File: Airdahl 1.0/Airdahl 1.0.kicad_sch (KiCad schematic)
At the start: 59 parts, among them J1 Conn_01x04, J2 DF40C-34DS-0.4V_58_, J3 DF40C-34DS-0.4V_58_, J4 USB_C_Receptacle_USB2.0_16P, SW1 SW_MEC_5E, SW2 SW_MEC_5E, U1 STM32F446RETx, U2 MCP2200-I-MQ, U3 LT1963AxST-3.3, Y1 ABM3B-8.000MHZ-12-D1X-T, Y2 ABS25-32.768KHZ-6-T, Y3 12MHz

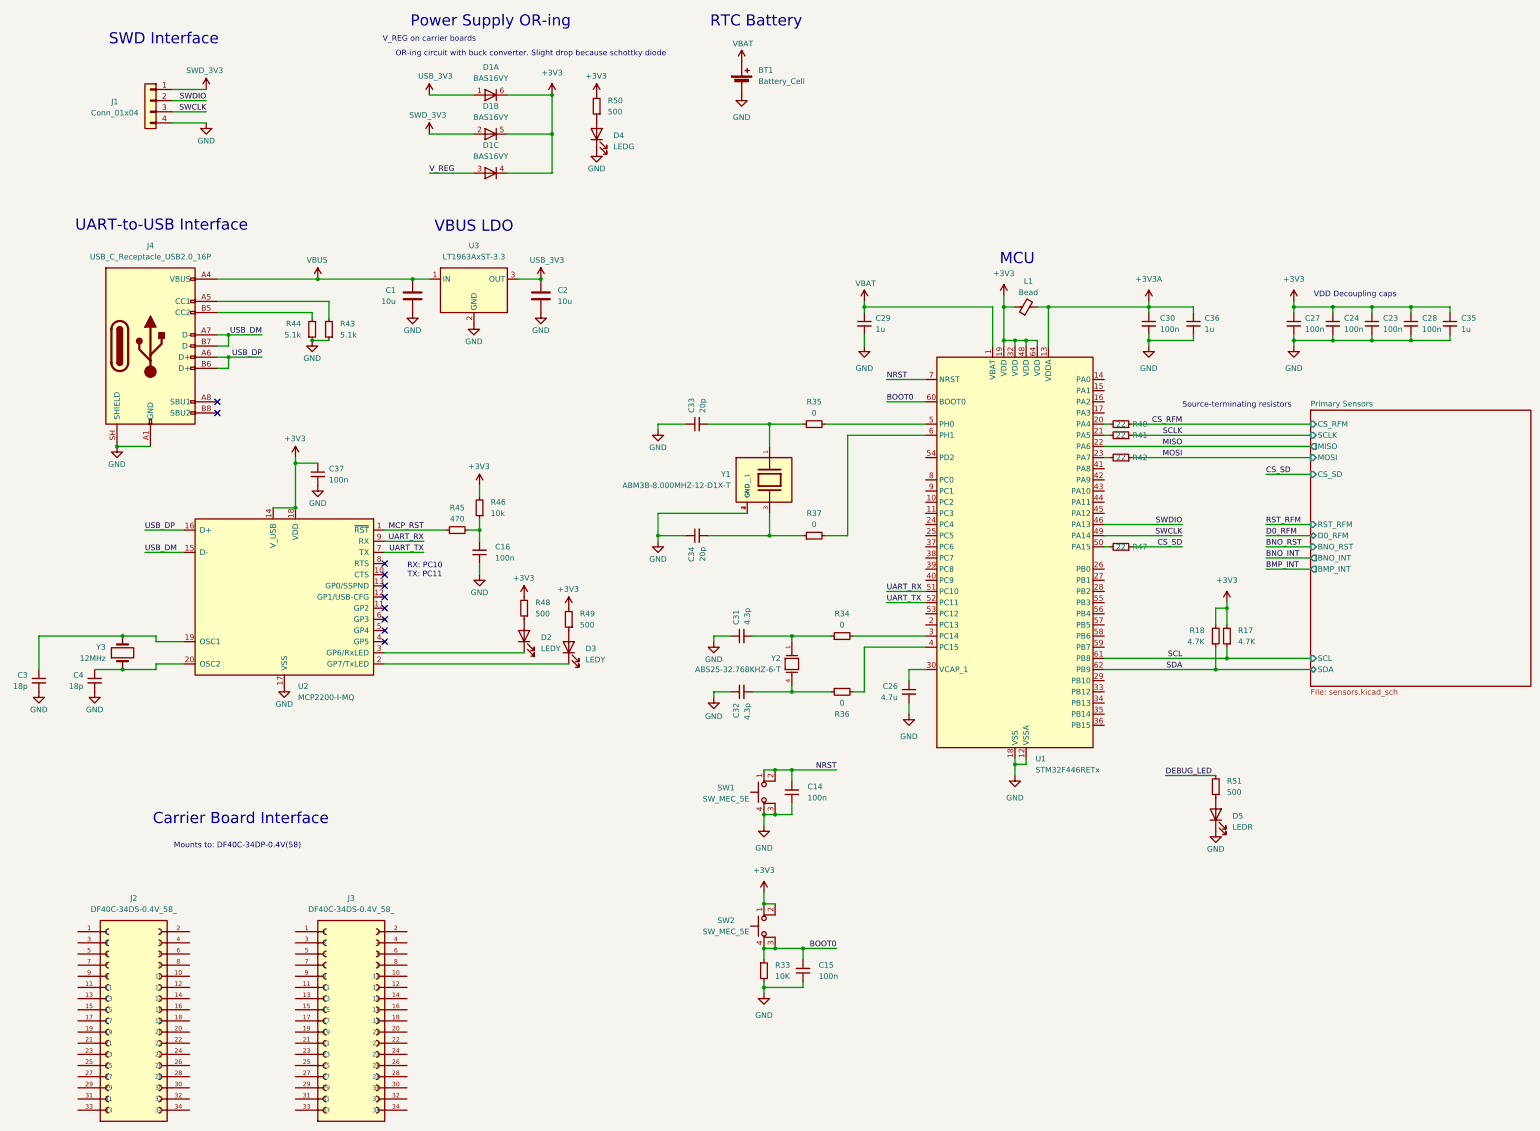
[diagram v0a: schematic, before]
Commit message: added to carrier board port pinout, need to add to mcu
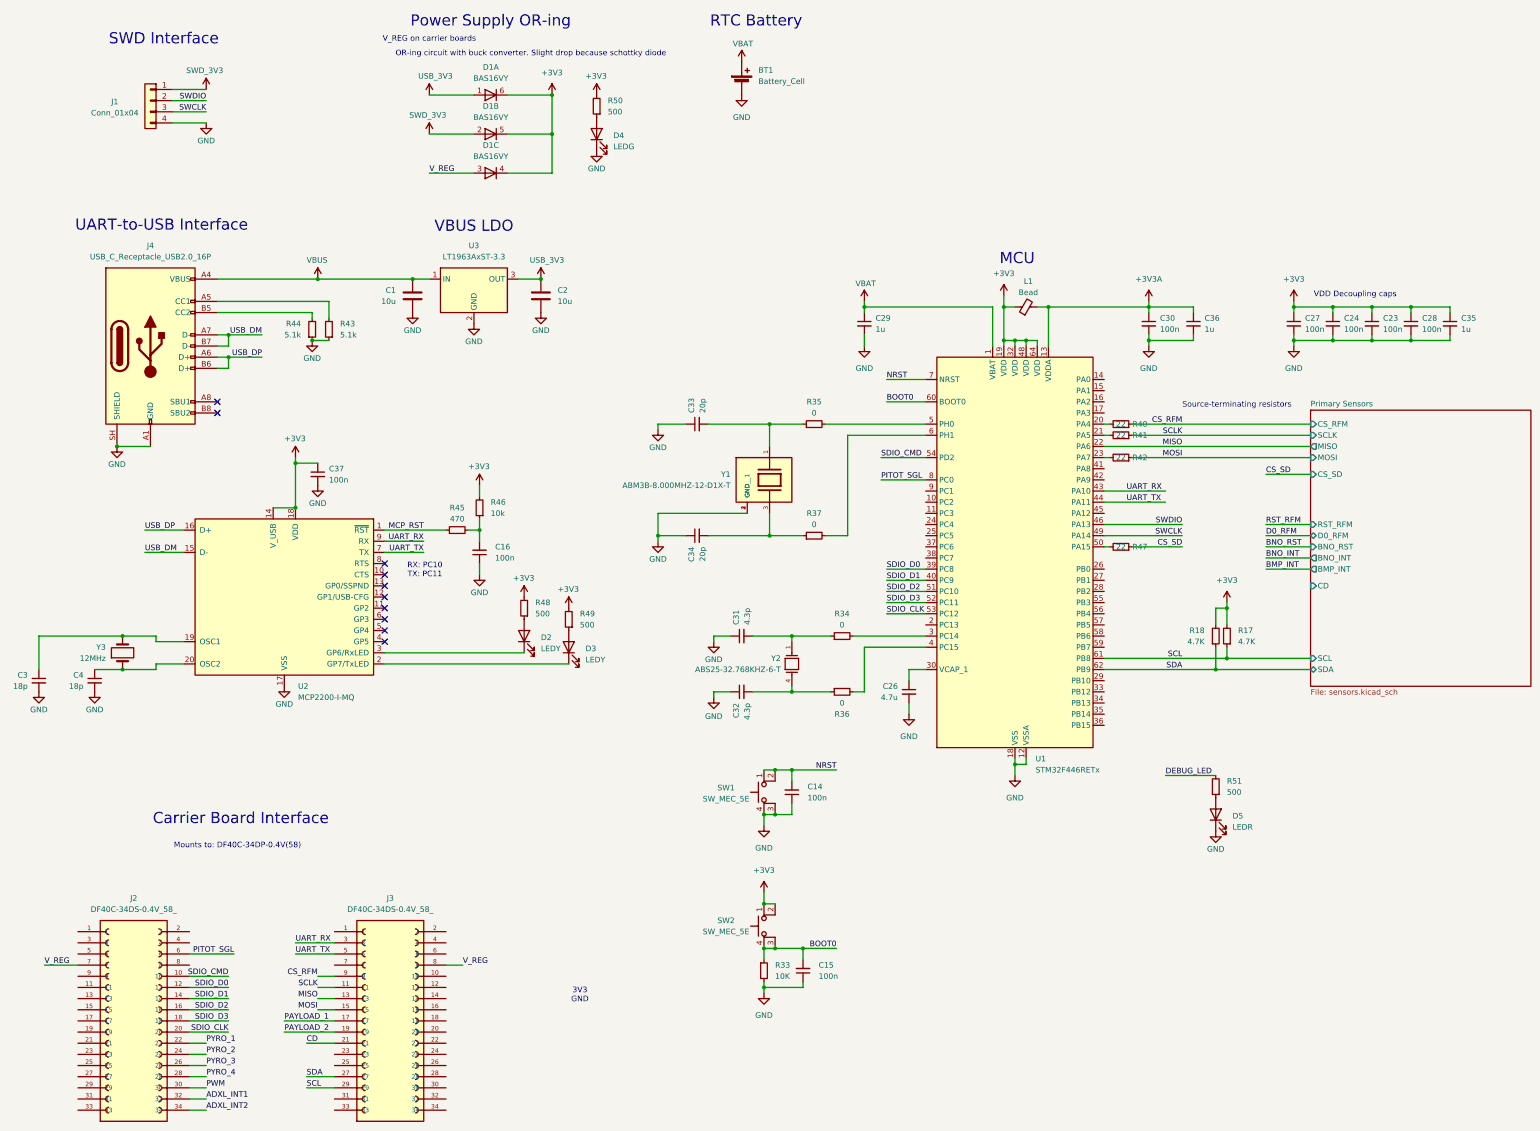
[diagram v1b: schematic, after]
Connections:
- net CS_RFM: now also J3.9
- net MISO: now also J3.13
- net MOSI: now also J3.15
- net SCL: now also J3.29
- net SCLK: now also J3.11
- net SDA: now also J3.27
- net UART_RX: now also J3.3, U1.43 (PA10); no longer U1.51 (PC10)
- net UART_TX: now also J3.5, U1.44 (PA11); no longer U1.52 (PC11)
- net V_REG: now also J2.7, J3.8
- net SDIO_CMD: now reaches J2.10
- net SDIO_CMD: now also U1.54 (PD2)
- net SDIO_D0: now reaches J2.12
- net SDIO_D0: now also U1.39 (PC8)
- net SDIO_D1: now reaches J2.14
- net SDIO_D1: now also U1.40 (PC9)
- net SDIO_D2: now reaches J2.16
- net SDIO_D2: now also U1.51 (PC10)
- net SDIO_D3: now reaches J2.18
- net SDIO_D3: now also U1.52 (PC11)
- net SDIO_CLK: now reaches J2.20
- net SDIO_CLK: now also U1.53 (PC12)
- net PYRO_1: now reaches J2.22
- net PYRO_2: now reaches J2.24
- net PYRO_3: now reaches J2.26
- net PYRO_4: now reaches J2.28
- net PWM: now reaches J2.30
- net ADXL_INT1: now reaches J2.32
- net ADXL_INT2: now reaches J2.34
- net PITOT_SGL: now reaches J2.6
- net PITOT_SGL: now also U1.8 (PC0)
- net PAYLOAD_1: now reaches J3.17
- net PAYLOAD_2: now reaches J3.19
- net CD: now reaches J3.21
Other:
- sheet Primary Sensors ports: added CD; removed none
- note added: "3V3 GND"
- moved on the sheet: J3

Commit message: MAIN BOARD SCHEMATIC REV1
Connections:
- net ADXL_INT1: now also U1.37 (PC6)
- net ADXL_INT2: now also U1.38 (PC7)
- net CD: now also U1.59 (PB7)
- net PAYLOAD_1: now also U1.42 (PA9)
- net PAYLOAD_2: now also U1.28 (PB2)
- net PWM: now also U1.41 (PA8)
- net PYRO_1: now also U1.35 (PB14)
- net PYRO_2: now also U1.34 (PB13)
- net PYRO_3: now also U1.33 (PB12)
- net PYRO_4: now also U1.29 (PB10)
- net PAYLOAD_A: now reaches U1.9 (PC1)
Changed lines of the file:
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@@
 	(wire
 		(pts
-			(xy 218.44 146.05) (xy 227.33 146.05)
+			(xy 217.17 146.05) (xy 227.33 146.05)
 		)
 		(stroke
@@
 	(wire
 		(pts
+			(xy 281.94 123.19) (xy 267.97 123.19)
+		)
+		(stroke
+			(width 0)
+			(type default)
+		)
+	)
+	(wire
+		(pts
 			(xy 337.82 85.09) (xy 337.82 83.82)
 		)
@@
 	(wire
 		(pts
+			(xy 217.17 138.43) (xy 227.33 138.43)
+		)
+		(stroke
+			(width 0)
+			(type default)
+		)
+	)
+	(wire
+		(pts
 			(xy 337.82 91.44) (xy 346.71 91.44)
 		)
@@
 	(wire
 		(pts
-			(xy 218.44 143.51) (xy 227.33 143.51)
+			(xy 217.17 143.51) (xy 227.33 143.51)
 		)
 		(stroke
@@
 	(wire
 		(pts
+			(xy 217.17 125.73) (xy 227.33 125.73)
+		)
+		(stroke
+			(width 0)
+			(type default)
+		)
+	)
+	(wire
+		(pts
+			(xy 281.94 148.59) (xy 267.97 148.59)
+		)
+		(stroke
+			(width 0)
+			(type default)
+		)
+	)
+	(wire
+		(pts
 			(xy 191.77 110.49) (xy 191.77 115.57)
 		)
@@
 	(wire
 		(pts
-			(xy 218.44 151.13) (xy 227.33 151.13)
+			(xy 217.17 151.13) (xy 227.33 151.13)
 		)
 		(stroke
@@
 	(wire
 		(pts
+			(xy 217.17 140.97) (xy 227.33 140.97)
+		)
+		(stroke
+			(width 0)
+			(type default)
+		)
+	)
+	(wire
+		(pts
+			(xy 281.94 171.45) (xy 267.97 171.45)
+		)
+		(stroke
+			(width 0)
+			(type default)
+		)
+	)
+	(wire
+		(pts
 			(xy 328.93 91.44) (xy 337.82 91.44)
 		)
@@
 	(wire
 		(pts
-			(xy 218.44 148.59) (xy 227.33 148.59)
+			(xy 217.17 148.59) (xy 227.33 148.59)
 		)
 		(stroke
@@
 	(wire
 		(pts
+			(xy 267.97 161.29) (xy 281.94 161.29)
+		)
+		(stroke
+			(width 0)
+			(type default)
+		)
+	)
+	(wire
+		(pts
 			(xy 274.32 138.43) (xy 285.75 138.43)
 		)
@@
 	(wire
 		(pts
-			(xy 218.44 153.67) (xy 227.33 153.67)
+			(xy 217.17 153.67) (xy 227.33 153.67)
 		)
 		(stroke
@@
 	(wire
 		(pts
+			(xy 281.94 176.53) (xy 267.97 176.53)
+		)
+		(stroke
+			(width 0)
+			(type default)
+		)
+	)
+	(wire
+		(pts
 			(xy 187.96 158.75) (xy 196.85 158.75)
 		)
@@
 	(wire
 		(pts
+			(xy 281.94 168.91) (xy 267.97 168.91)
+		)
+		(stroke
+			(width 0)
+			(type default)
+		)
+	)
+	(wire
+		(pts
 			(xy 328.93 90.17) (xy 328.93 91.44)
 		)
@@
 	(wire
 		(pts
+			(xy 281.94 120.65) (xy 267.97 120.65)
+		)
+		(stroke
+			(width 0)
+			(type default)
+		)
+	)
+	(wire
+		(pts
 			(xy 26.67 233.68) (xy 34.29 233.68)
+		)
+		(stroke
+			(width 0)
+			(type default)
+		)
+	)
+	(wire
+		(pts
+			(xy 281.94 173.99) (xy 267.97 173.99)
 		)
 		(stroke
@@
 		)
 	)
+	(label "ADXL_INT2"
+		(at 217.17 140.97 0)
+		(effects
+			(font
+				(size 1.27 1.27)
+			)
+			(justify left bottom)
+		)
+	)
 	(label "USB_DP"
 		(at 49.53 134.62 0)
@@
 		)
 	)
+	(label "PYRO_2"
+		(at 281.94 173.99 180)
+		(effects
+			(font
+				(size 1.27 1.27)
+			)
+			(justify right bottom)
+		)
+	)
 	(label "CD"
 		(at 86.36 251.46 0)
@@
 	)
 	(label "SDIO_D2"
-		(at 218.44 148.59 0)
+		(at 217.17 148.59 0)
 		(effects
 			(font
@@
 		)
 	)
+	(label "PYRO_3"
+		(at 281.94 171.45 180)
+		(effects
+			(font
+				(size 1.27 1.27)
+			)
+			(justify right bottom)
+		)
+	)
 	(label "MISO"
 		(at 285.75 115.57 180)
@@
 		)
 	)
+	(label "ADXL_INT1"
+		(at 217.17 138.43 0)
+		(effects
+			(font
+				(size 1.27 1.27)
+			)
+			(justify left bottom)
+		)
+	)
+	(label "CD"
+		(at 281.94 161.29 180)
+		(effects
+			(font
+				(size 1.27 1.27)
+			)
+			(justify right bottom)
+		)
+	)
 	(label "V_REG"
 		(at 26.67 233.68 0)
@@
 		)
 	)
+	(label "PAYLOAD_2"
+		(at 281.94 148.59 180)
+		(effects
+			(font
+				(size 1.27 1.27)
+			)
+			(justify right bottom)
+		)
+	)
 	(label "SDIO_CLK"
 		(at 68.58 248.92 180)
@@
 	)
 	(label "SDIO_CLK"
-		(at 218.44 153.67 0)
+		(at 217.17 153.67 0)
 		(effects
 			(font
@@
 		)
 	)
+	(label "PWM"
+		(at 281.94 120.65 180)
+		(effects
+			(font
+				(size 1.27 1.27)
+			)
+			(justify right bottom)
+		)
+	)
 	(label "V_REG"
 		(at 114.3 53.34 0)
@@
 		)
 	)
+	(label "PAYLOAD_A"
+		(at 217.17 125.73 0)
+		(effects
+			(font
+				(size 1.27 1.27)
+			)
+			(justify left bottom)
+		)
+	)
 	(label "CS_RFM"
 		(at 88.9 236.22 180)
@@
 		)
 	)
+	(label "PAYLOAD_1"
+		(at 281.94 123.19 180)
+		(effects
+			(font
+				(size 1.27 1.27)
+			)
+			(justify right bottom)
+		)
+	)
 	(label "CS_SD"
 		(at 285.75 138.43 180)
@@
 	)
 	(label "SDIO_D3"
-		(at 218.44 151.13 0)
-		(effects
-			(font
-				(size 1.27 1.27)
-			)
-			(justify left bottom)
+		(at 217.17 151.13 0)
+		(effects
+			(font
+				(size 1.27 1.27)
+			)
+			(justify left bottom)
+		)
+	)
+	(label "PYRO_4"
+		(at 281.94 168.91 180)
+		(effects
+			(font
+				(size 1.27 1.27)
+			)
+			(justify right bottom)
 		)
 	)
@@
 	)
 	(label "SDIO_D0"
-		(at 218.44 143.51 0)
+		(at 217.17 143.51 0)
 		(effects
 			(font
@@
 	)
 	(label "SDIO_D1"
-		(at 218.44 146.05 0)
+		(at 217.17 146.05 0)
 		(effects
 			(font
@@
 		(effects
 			(font
+				(size 1.27 1.27)
+			)
+			(justify right bottom)
+		)
+	)
+	(label "PYRO_1"
+		(at 281.94 176.53 180)
+		(effects
+			(font

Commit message: stoning my cap
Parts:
- removed D1: BAS16VY, Package_TO_SOT_SMD:SOT-363_SC-70-6, symbol Diode:BAS16VY
- added D1, D6: RB496EATR, DIO_FTZ_ROM, symbol RB496EATR:RB496EATR
- added R58, R59, R60, R61, R62: 22, Resistor_SMD:R_0402_1005Metric, symbol Device:R_Small
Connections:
- net +3V3: now also D1.4, D1.5, D6.4, D6.5
- net SDIO_CLK: now also R61.2; no longer J2.20, U1.53 (PC12)
- net SDIO_CMD: now also R62.2; no longer J2.10, U1.54 (PD2)
- net SDIO_D0: now also R47.2; no longer J2.12, U1.39 (PC8)
- net SDIO_D1: now also R58.2; no longer J2.14, U1.40 (PC9)
- net SDIO_D2: now also R59.2; no longer J2.16, U1.51 (PC10)
- net SDIO_D3: now also R60.2; no longer J2.18, U1.52 (PC11)
- net SWD_3V3: now also D1.3
- net USB_3V3: now also D1.1
- net V_REG: now also D6.1
- net at U1.50 (PA15): no longer R47.2
- net CS_SD: no longer names the net of R47.1
- net CS_SD: now also U1.39 (PC8)
- new net: R61.1, U1.53 (PC12)
- new net: R58.1, U1.40 (PC9)
- new net: R59.1, U1.51 (PC10)
- new net: R60.1, U1.52 (PC11)
- new net: R62.1, U1.54 (PD2)
- no-connect marks 10 -> 13
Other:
- sheet Primary Sensors ports: added SDIO_CLK, SDIO_CMD, SDIO_D0, SDIO_D1, SDIO_D2, SDIO_D3; removed CS_SD
- moved on the sheet: C33, C34, D2, D3, D4, R35, R37, R48, R49, R50, Y1

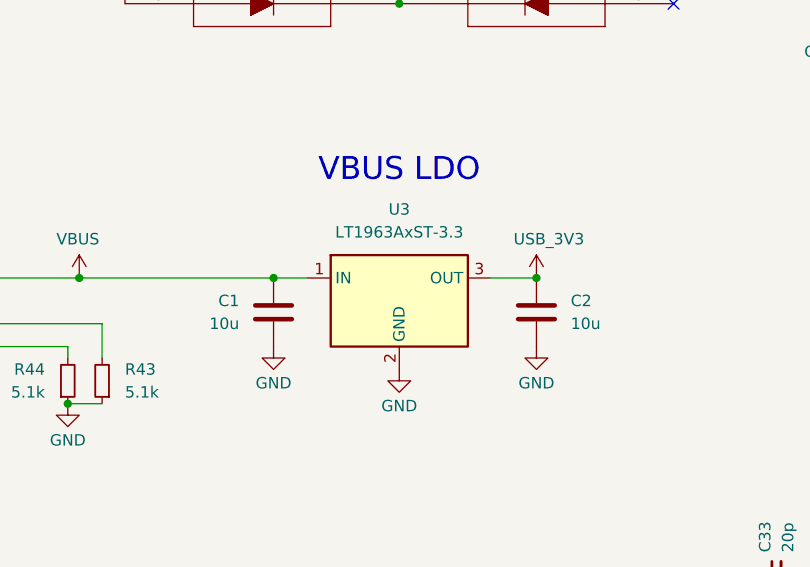
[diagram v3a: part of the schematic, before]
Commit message: added 5v power to ace carrier for pitot tube, dsub-9 pinouts, voltage divider for pitot sensor signal, changed vbus ldo on mainboard to ncp1117
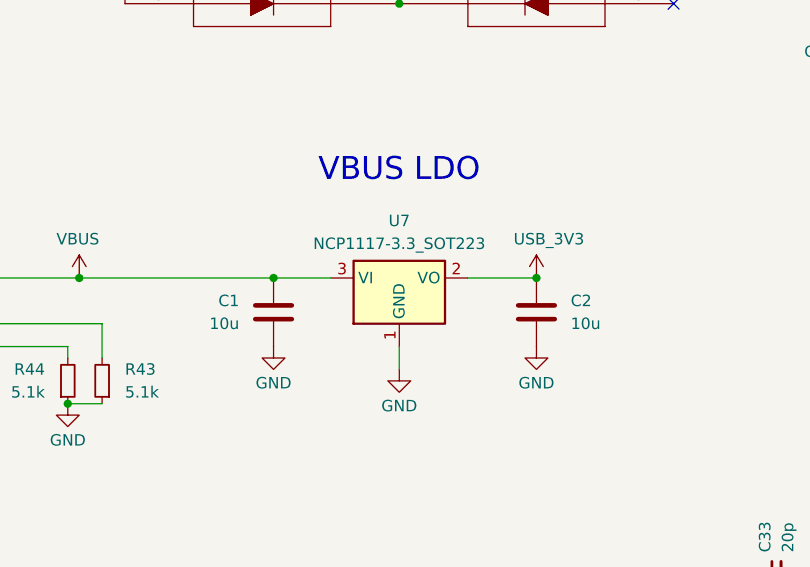
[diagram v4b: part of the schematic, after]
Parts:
- removed U3: LT1963AxST-3.3, Package_TO_SOT_SMD:SOT-223-3_TabPin2, symbol Regulator_Linear:LT1963AxST-3.3
- added U7: NCP1117-3.3_SOT223, Package_TO_SOT_SMD:SOT-223-3_TabPin2, symbol Regulator_Linear:NCP1117-3.3_SOT223
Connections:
- net GND: now also U7.1 (GND)
- net USB_3V3: now also U7.2 (VO)
- net VBUS: now also U7.3 (VI)
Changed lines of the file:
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@@
 	(wire
 		(pts
-			(xy 110.49 77.47) (xy 114.3 77.47)
+			(xy 110.49 77.47) (xy 116.84 77.47)
 		)
 		(stroke
@@
 	(wire
 		(pts
+			(xy 124.46 85.09) (xy 124.46 87.63)
+		)
+		(stroke
+			(width 0)
+			(type default)
+		)
+	)
+	(wire
+		(pts
 			(xy 242.57 83.82) (xy 242.57 92.71)
 		)
@@
 	(wire
 		(pts
+			(xy 132.08 77.47) (xy 139.7 77.47)
+		)
+		(stroke
+			(width 0)
+			(type default)
+		)
+	)
+	(wire
+		(pts
 			(xy 196.85 171.45) (xy 196.85 170.18)
 		)
@@
 	(wire
 		(pts
-			(xy 134.62 77.47) (xy 139.7 77.47)
-		)
-		(stroke
-			(width 0)
-			(type default)
-		)
-	)
-	(wire
-		(pts
 			(xy 104.14 139.7) (xy 113.03 139.7)
 		)
@@
 	)
 	(symbol
-		(lib_id "Regulator_Linear:LT1963AxST-3.3")
-		(at 124.46 80.01 0)
-		(unit 1)
-		(body_style 1)
-		(exclude_from_sim no)
-		(in_bom yes)
-		(on_board yes)
-		(in_pos_files yes)
-		(dnp no)
-		(fields_autoplaced yes)
-		(property "Reference" "U3"
-			(at 124.46 69.85 0)
-			(show_name no)
-			(do_not_autoplace no)
-			(effects
-				(font
-					(size 1.27 1.27)
-				)
-			)
-		)
-		(property "Value" "LT1963AxST-3.3"
-			(at 124.46 72.39 0)
-			(show_name no)
-			(do_not_autoplace no)
-			(effects
-				(font
-					(size 1.27 1.27)
-				)
-			)
-		)
-		(property "Footprint" "Package_TO_SOT_SMD:SOT-223-3_TabPin2"
-			(at 124.46 91.44 0)
-			(hide yes)
-			(show_name no)
-			(do_not_autoplace no)
-			(effects
-				(font
-					(size 1.27 1.27)
-				)
-			)
-		)
-		(property "Datasheet" "https://www.analog.com/media/en/technical-documentation/data-sheets/1963aff.pdf"
-			(at 124.46 93.98 0)
-			(hide yes)
-			(show_name no)
-			(do_not_autoplace no)
-			(effects
-				(font
-					(size 1.27 1.27)
-				)
-			)
-		)
-		(property "Description" "3.3V, 1.5A, Low Noise, Fast Transient Response LDO Regulator, SOT-223"
-			(at 124.46 80.01 0)
-			(hide yes)
-			(show_name no)
-			(do_not_autoplace no)
-			(effects
-				(font
-					(size 1.27 1.27)
-				)
-			)
-		)
-		(pin "1"
-		)
-		(pin "3"
-		)
-		(pin "2"
-		)
-		(instances
-			(project "Airdahl 1.0"
-				(path "/e2c992a5-0f37-48ff-88a4-7c40cfcda45e"
-					(reference "U3")
-					(unit 1)
-				)
-			)
-		)
-	)
-	(symbol
 		(lib_id "Device:C_Small")
 		(at 288.29 87.63 0)
@@
 					(unit 1)
 				)
+			)
+		)
+	)
+	(symbol
+		(lib_id "Regulator_Linear:NCP1117-3.3_SOT223")
+		(at 124.46 77.47 0)
+		(unit 1)
+		(body_style 1)
+		(exclude_from_sim no)
+		(in_bom yes)
+		(on_board yes)
+		(in_pos_files yes)
+		(dnp no)
+		(fields_autoplaced yes)
+		(property "Reference" "U7"
+			(at 124.46 71.12 0)
+			(show_name no)
+			(do_not_autoplace no)
+			(effects
+				(font
+					(size 1.27 1.27)
+				)
+			)
+		)
+		(property "Value" "NCP1117-3.3_SOT223"
+			(at 124.46 73.66 0)
+			(show_name no)
+			(do_not_autoplace no)
+			(effects
+				(font
+					(size 1.27 1.27)
+				)
+			)
+		)
+		(property "Footprint" "Package_TO_SOT_SMD:SOT-223-3_TabPin2"
+			(at 124.46 72.39 0)
+			(hide yes)
+			(show_name no)
+			(do_not_autoplace no)
+			(effects
+				(font
+					(size 1.27 1.27)
+				)
+			)
+		)
+		(property "Datasheet" "http://www.onsemi.com/pub_link/Collateral/NCP1117-D.PDF"
+			(at 127 83.82 0)
+			(hide yes)
+			(show_name no)
+			(do_not_autoplace no)
+			(effects
+				(font
+					(size 1.27 1.27)
+				)
+			)
+		)
+		(property "Description" "1A Low drop-out regulator, Fixed Output 3.3V, SOT-223"
+			(at 124.46 77.47 0)
+			(hide yes)
+			(show_name no)
+			(do_not_autoplace no)
+			(effects
+				(font
+					(size 1.27 1.27)
+				)
+			)
+		)
+		(pin "3"
+		)
+		(pin "2"
+		)
+		(pin "1"
+		)
+		(instances
+			(project "Airdahl 1.0"
+				(path "/e2c992a5-0f37-48ff-88a4-7c40cfcda45e"
+					(reference "U7")
+					(unit 1)
+				)
